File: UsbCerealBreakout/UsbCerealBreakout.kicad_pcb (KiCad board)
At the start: 2 copper layers, 8.2 x 5 mm, 3 parts, among them J1 Serial Connector, J2 USB_C_Data_Output, P1 USB_C_Plug

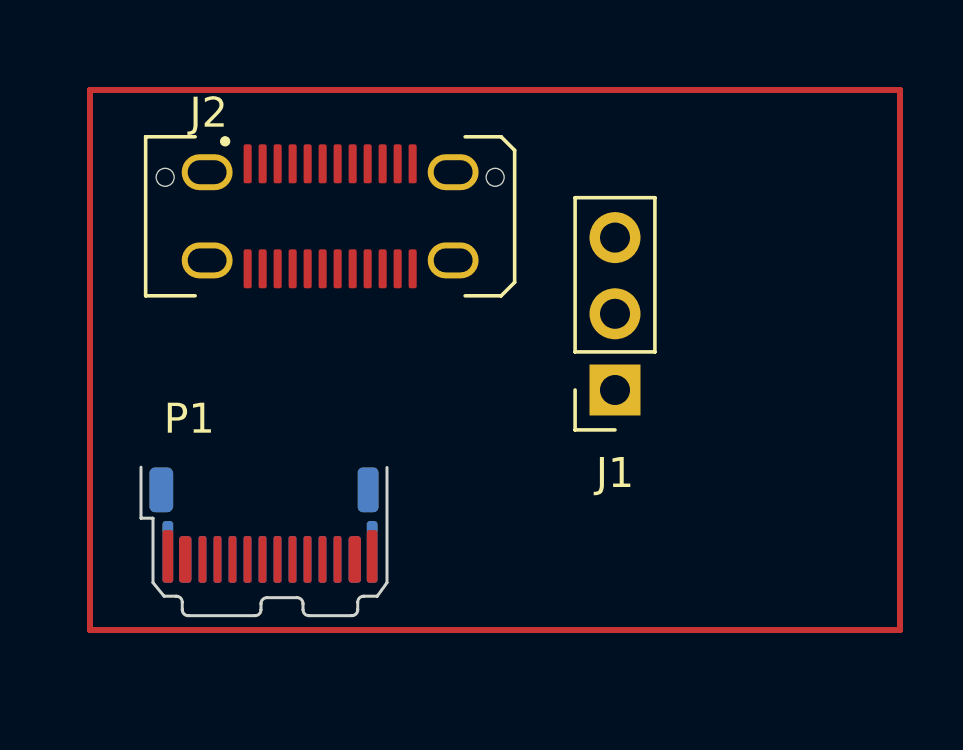
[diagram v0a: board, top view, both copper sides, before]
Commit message: Route the PCB, it may have some DRC issues and incorrect thickness for the USB-C plug connector
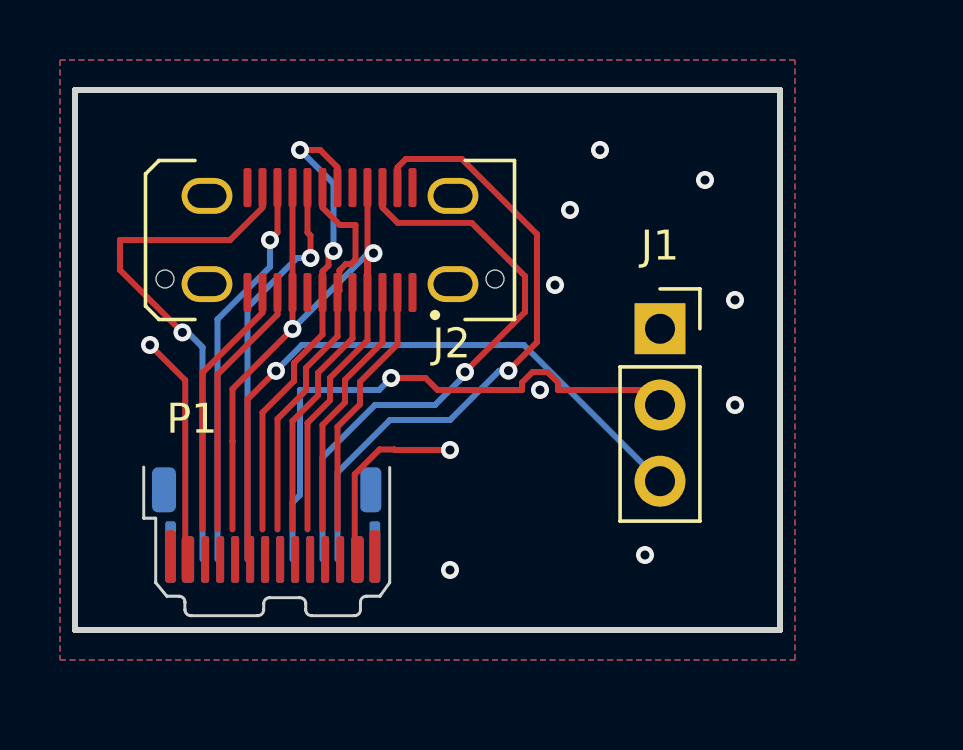
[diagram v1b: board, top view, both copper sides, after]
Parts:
- moved J1 2.53 mm to (142.0, 72.5), turned to 0 degrees
- moved J2 0.79 mm to (131.0, 69.5), turned to 180 degrees
- moved P1 0.09 mm to (129.1, 79.0)
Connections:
- J2 pad SH: unconnected-(J2-SHIELD-PadSH) -> GND
- P1 pad SH: unconnected-(P1-SHIELD-PadSH) -> GND
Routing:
- net Net-(J2-VBUS-PadA4): track 0.00 -> 29.7 mm, vias 0 -> 2
- net Net-(J1-Pin_3): track 0.00 -> 21.7 mm, vias 0 -> 1
- net Net-(J2-RX1+): track 0.00 -> 21.4 mm, vias 0 -> 1
- net Net-(J2-RX1-): track 0.00 -> 19.8 mm, vias 0 -> 1
- net Net-(J1-Pin_2): track 0.00 -> 19.1 mm, vias 0 -> 1
- net Net-(J2-TX2+): track 0.00 -> 17.8 mm, vias 0 -> 1
- net Net-(P1-D-): track 0.00 -> 16.2 mm, vias 0 -> 2
- net GND: track 0.00 -> 14.0 mm, vias 0 -> 11
- net Net-(P1-D+): track 0.00 -> 13.8 mm
- net Net-(J2-CC2): track 0.00 -> 13.6 mm, vias 0 -> 1
- net Net-(J2-TX2-): track 0.00 -> 13.2 mm, vias 0 -> 1
- net Net-(J2-TX1-): track 0.00 -> 8.73 mm
- net Net-(J2-TX1+): track 0.00 -> 8.73 mm
- net Net-(J2-RX2-): track 0.00 -> 8.73 mm
- net Net-(J2-RX2+): track 0.00 -> 8.73 mm
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- added copper zone on B.Cu, net GND
- added copper zone on F.Cu, net GND
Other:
- board size 8.2 x 5 mm -> 23.5 x 18 mm

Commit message: fixed some stuff
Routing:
- net GND: track 14.0 -> 32.9 mm, vias 11 -> 10
- net (no net): track 0.00 -> 9.73 mm
- net Net-(J2-VBUS-PadA4): track 29.7 -> 36.5 mm, vias 2 -> 4
- net Net-(J2-TX2+): track 17.8 -> 23.4 mm, vias 1 -> 3
- net Net-(J2-CC1): track 8.73 -> 9.76 mm
- net Net-(P1-D-): track 16.2 -> 17.3 mm
- net Net-(J2-TX1-): track 8.73 -> 9.76 mm
- net Net-(J2-RX2-): track 8.73 -> 9.76 mm
- net Net-(J2-RX2+): track 8.73 -> 9.76 mm
- net Net-(P1-D+): track 13.8 -> 14.9 mm
- net Net-(J2-TX1+): track 8.73 -> 9.76 mm
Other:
- board size 23.5 x 18 mm -> 23.5 x 19 mm

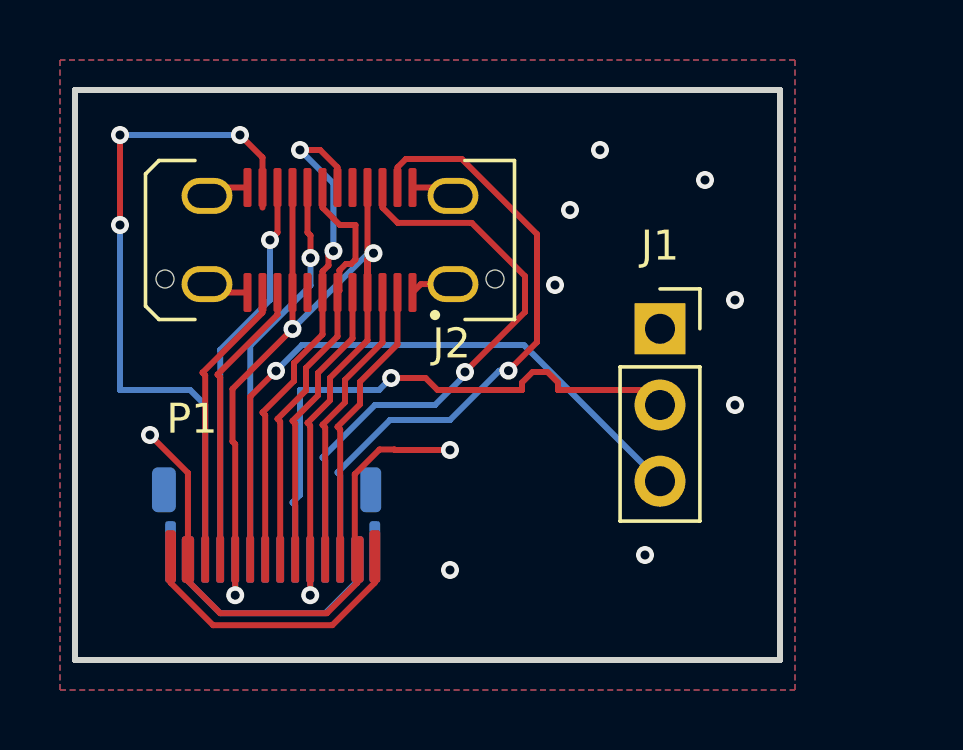
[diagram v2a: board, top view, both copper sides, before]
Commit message: Removed unnecessary trace
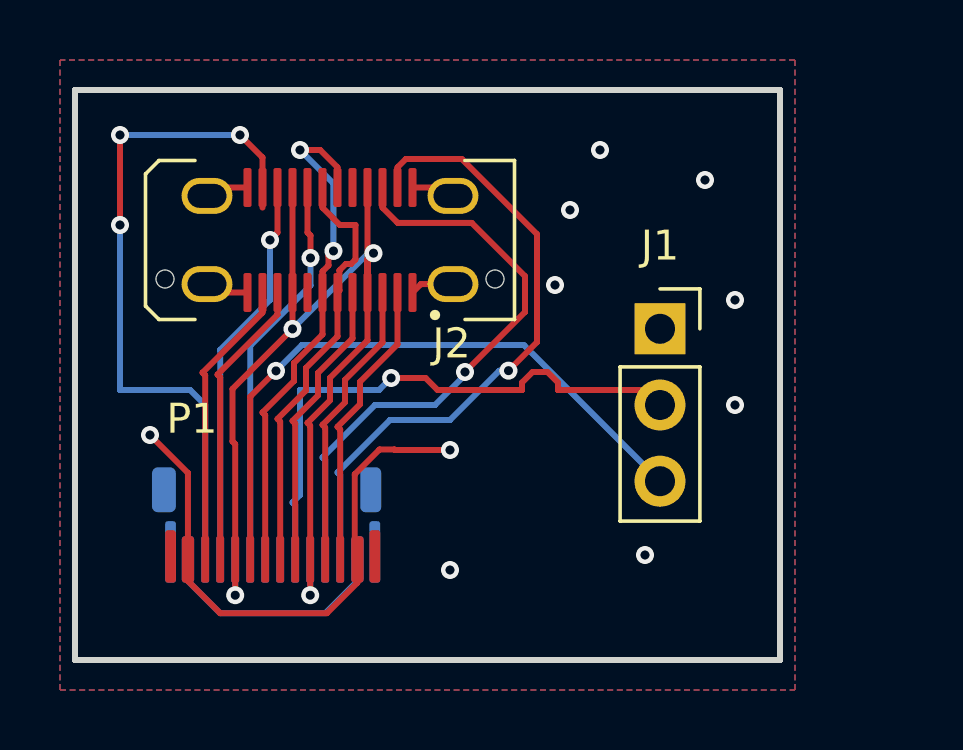
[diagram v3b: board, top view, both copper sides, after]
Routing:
- net (no net): track 9.73 -> 0.00 mm
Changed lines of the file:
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@@
 		(capping no)
 		(filling no)
-		(zone_defaults)
 		(pcbplotparams
 			(layerselection 0x00000000_00000000_55555555_5755f5ff)
@@
 			(outputformat 1)
 			(mirror no)
-			(drillshape 1)
+			(drillshape 0)
 			(scaleselection 1)
-			(outputdirectory "")
+			(outputdirectory "build")
 		)
 	)
@@
 	)
 	(segment
-		(start 131.077499 82.34)
-		(end 127.102501 82.34)
-		(width 0.2)
-		(layer "F.Cu")
-		(net "")
-	)
-	(segment
-		(start 132.495 80.0475)
-		(end 132.495 80.922499)
-		(width 0.2)
-		(layer "F.Cu")
-		(net "")
-	)
-	(segment
-		(start 127.102501 82.34)
-		(end 125.685 80.922499)
-		(width 0.2)
-		(layer "F.Cu")
-		(net "")
-	)
-	(segment
-		(start 125.685 80.922499)
-		(end 125.685 80.0475)
-		(width 0.2)
-		(layer "F.Cu")
-		(net "")
-	)
-	(segment
-		(start 132.495 80.922499)
-		(end 131.077499 82.34)
-		(width 0.2)
-		(layer "F.Cu")
-		(net "")
-	)
-	(segment
